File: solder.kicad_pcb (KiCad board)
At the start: 2 copper layers, 53 x 36 mm, 17 parts, among them M1 Motor_DC, SW1 SW_Push, SW2 SW_Push

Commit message: fixed routing
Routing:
- net Net-(BT1-+): track 120.3 -> 126.8 mm
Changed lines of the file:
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@@
 	)
 	(segment
-		(start 76.089 80.45605)
-		(end 76.089 79.54395)
+		(start 76.73395 81.101)
+		(end 91.738892 81.101)
+		(width 0.2)
+		(layer "F.Cu")
+		(net 1)
+	)
+	(segment
+		(start 91.738892 81.101)
+		(end 104.301 68.538892)
 		(width 0.2)
 		(layer "F.Cu")
@@
 	)
 	(segment
-		(start 76.73395 81.101)
-		(end 76.089 80.45605)
-		(width 0.2)
-		(layer "F.Cu")
-		(net 1)
-	)
-	(segment
-		(start 96.5 63.5)
-		(end 100.339892 63.5)
+		(start 104.301 68.538892)
+		(end 104.301 67.461108)
 		(width 0.2)
 		(layer "F.Cu")
@@
 	)
 	(segment
-		(start 76.089 79.54395)
-		(end 86.985 68.64795)
+		(start 100.339892 63.5)
+		(end 96.5 63.5)
+		(width 0.2)
+		(layer "F.Cu")
+		(net 1)
+	)
+	(segment
+		(start 76.089 80.45605)
+		(end 76.73395 81.101)
 		(width 0.2)
 		(layer "F.Cu")
@@
 	)
 	(segment
-		(start 91.738892 81.101)
-		(end 76.73395 81.101)
-		(width 0.2)
-		(layer "F.Cu")
-		(net 1)
-	)
-	(segment
 		(start 103 52.5)
 		(end 96.5 52.5)
@@
 	)
 	(segment
-		(start 86.985 68.64795)
-		(end 86.985 60)
+		(start 104.301 62.199)
+		(end 104.301 53.801)
 		(width 0.2)
 		(layer "F.Cu")
@@
 	)
 	(segment
-		(start 104.301 62.199)
-		(end 104.301 53.801)
+		(start 76.089 79.54395)
+		(end 76.089 80.45605)
+		(width 0.2)
+		(layer "F.Cu")
+		(net 1)
+	)
+	(segment
+		(start 86.985 68.64795)
+		(end 76.089 79.54395)
+		(width 0.2)
+		(layer "F.Cu")
+		(net 1)
+	)
+	(segment
+		(start 96.5 63.5)
+		(end 103 63.5)
+		(width 0.2)
+		(layer "F.Cu")
+		(net 1)
+	)
+	(segment
+		(start 104.301 67.461108)
+		(end 100.339892 63.5)
 		(width 0.2)
 		(layer "F.Cu")
@@
 	)
 	(segment
-		(start 104.301 67.461108)
-		(end 104.301 68.538892)
+		(start 86.985 60)
+		(end 86.985 68.64795)
 		(width 0.2)
 		(layer "F.Cu")
-		(net 1)
-	)
-	(segment
-		(start 104.301 68.538892)
-		(end 91.738892 81.101)
-		(width 0.2)
-		(layer "F.Cu")
-		(net 1)
-	)
-	(segment
-		(start 100.339892 63.5)
-		(end 104.301 67.461108)
-		(width 0.2)
-		(layer "F.Cu")

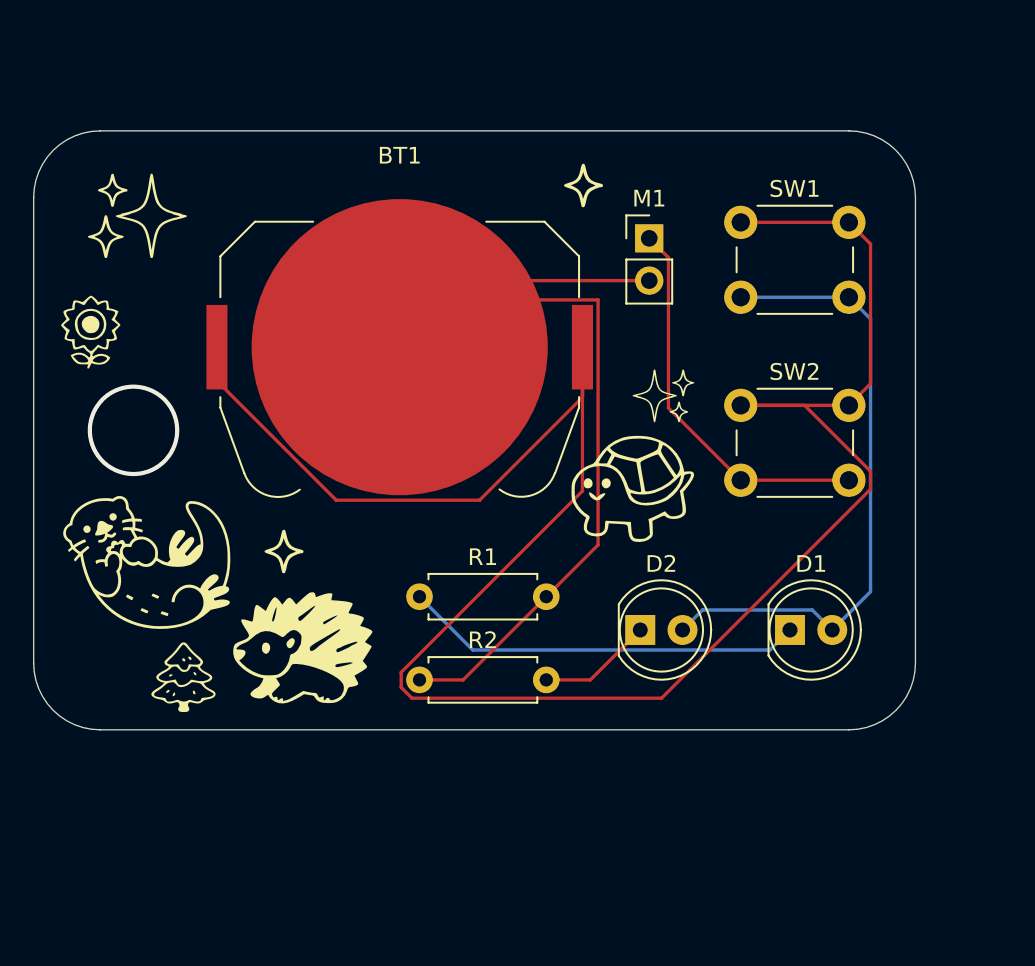
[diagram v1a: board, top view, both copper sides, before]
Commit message: added to back silkscreen, rotated the pcb, added name
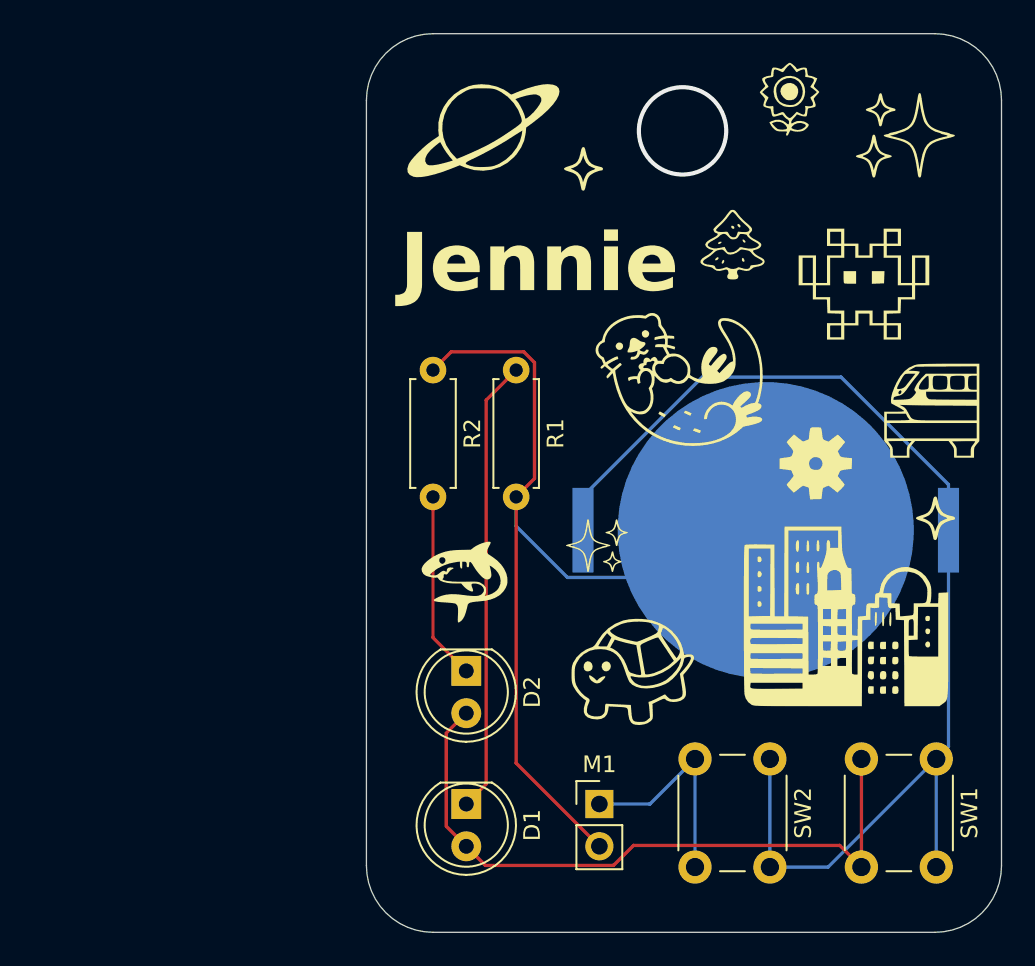
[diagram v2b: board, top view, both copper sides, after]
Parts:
- removed the G*** at (69.0, 72.0)
- added G***: LOGO, LOGO, F.Cu at (87.0, 49.0)
- added G***: LOGO, LOGO, B.Cu at (87.0, 45.0)
- added G***: LOGO, LOGO, B.Cu at (106.0, 49.0)
- added G***: LOGO, LOGO, B.Cu at (101.0, 90.0)
- added G***: LOGO, LOGO, B.Cu at (107.0, 88.0)
- added G***: LOGO, LOGO, B.Cu at (84.0, 91.0)
- added G***: LOGO, LOGO, B.Cu at (80.0, 57.0)
- added G***: LOGO, LOGO, B.Cu at (80.0, 74.0)
- added G***: LOGO, LOGO, B.Cu at (99.0, 53.0)
- added G***: LOGO, LOGO, B.Cu at (82.0, 66.0)
- added G***: LOGO, LOGO, B.Cu at (80.0, 48.0)
- added G***: LOGO, LOGO, B.Cu at (100.0, 46.0)
- added G***: LOGO, LOGO, B.Cu at (105.0, 56.0)
- added G***: LOGO, LOGO, B.Cu at (88.0, 83.0)
- added G***: LOGO, LOGO, F.Cu at (80.0, 74.0)
- added G***: LOGO, LOGO, F.Cu at (104.0, 56.0)
- added G***: LOGO, LOGO, F.Cu at (103.0, 76.0)
- added G***: LOGO, LOGO, F.Cu at (81.0, 47.0)
- added G***: LOGO, LOGO, F.Cu at (108.0, 64.0)
- added G***: LOGO, LOGO, F.Cu at (101.0, 67.0)
- BT1, G***: moved to B.Cu
- moved G*** 46.4 mm to (106.2, 47.2)
- moved G*** 44.3 mm to (99.0, 45.0)
- moved G*** 42.0 mm to (96.0, 54.0)
- moved SW1 34.3 mm to (108.2, 84.8), turned to -90 degrees
- moved M1 34.1 mm to (88.0, 87.5)
- moved G*** 33.8 mm to (93.0, 62.0)
- moved G*** 30.4 mm to (91.0, 56.0), turned to 180 degrees
- moved G*** 29.1 mm to (108.2, 70.0)
- moved BT1 24.6 mm to (98.0, 71.0), turned to 180 degrees
- moved D1 22.1 mm to (80.0, 87.5), turned to -90 degrees
- moved SW2 21.3 mm to (98.2, 84.8), turned to -90 degrees
- moved R2 18.6 mm to (78.0, 61.4), turned to -90 degrees
- moved R1 14.8 mm to (83.0, 61.4), turned to -90 degrees
- moved G*** 11.0 mm to (90.0, 80.0)
- moved D2 10.7 mm to (80.0, 79.5), turned to -90 degrees
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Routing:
- net Net-(BT1-+): track 126.8 -> 72.1 mm
- net Net-(M1-+): track 23.3 -> 13.4 mm
- net Net-(D2-K): track 6.89 -> 11.3 mm
- net Net-(D1-K): track 24.1 -> 27.3 mm
- net Net-(D1-A): track 38.0 -> 40.8 mm
- net Net-(BT1--): track 58.6 -> 57.6 mm
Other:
- board size 53 x 36 mm -> 38.2 x 54 mm
- board text added: "Jennie"
